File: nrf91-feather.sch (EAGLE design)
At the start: 59 parts, among them J1 CON-USB-1050170001, J2 CON-HEADER-1X12-MALE-PIN, J3 CON-HEADER-1X16-MALE-PIN, J4 1909763-1, J5 104224-0820, J6 CON-S2B-PH-SM4-TB(LF)(SN), J9 CON-0002, Q1 MOSFET-P-SC89, Q2 MOSFET-DUAL-COMP-VMT6, Q3 MOSFET-P-30V-4.3A-SOT23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

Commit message: Adding parallel LDO for low power op. (without need to shut everything off)
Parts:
- removed R4: 100k, wolff-den:RES-100K-1%-0402
- removed R5, R6: 20k, wolff-den:RES-20K-1%-0402
- removed U5: IC-BAV70S, wolff-den:IC-BAV70S
- removed Y1: XTAL-ABS07AIG-32.768KHZ-7-T, wolff-den:XTAL-ABS07AIG-32.768KHZ-7-T
- added C12: 1u, wolff-den:CAP-1U-25V-0402
- C2: value 0.1u -> 1u; device wolff-den:CAP-0.1U-50V-0402 -> wolff-den:CAP-1U-25V-0402
- Q1: value MOSFET-P-SC89 -> MOSFET-N-SC89; device wolff-den:MOSFET-P-SC89 -> wolff-den:MOSFET-N-SC89
- R1: value 100k -> 1M; device wolff-den:RES-100K-1%-0402 -> wolff-den:RES-1M-5%-0402
- U2: value IC-PCF85063ATL/1 -> IC-CP2102N-A02-GQFN20R; device wolff-den:IC-PCF85063ATL/1 -> wolff-den:IC-CP2102N-A02-GQFN20R
- U4: value IC-BAV70S -> (none); device wolff-den:IC-BAV70S -> wolff-den:POWER-VREG-EN-DFN4-1X1
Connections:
- removed net 3V3_EN: R2.2, U3.EN, U4G$1.C, U4G$2.C, U5G$1.C
- removed net N$10: U2.OSCI, Y1.2
- removed net N$18: U2.OSCO, Y1.1
- removed net P0.05/RTC_SCL: R6.1, U1.P0.05, U2.SCL
- removed net P0.06/RTC_SDA: R5.1, U1.P0.06, U2.SDA
- removed net RTC_INT: Q1.G, R4.1, U2.!INT
- removed net RTC_PS_EN: Q1.D, U4G$1.A1
- new net D+: J1.D+, U2.D+
- new net D-: J1.D-, U2.D-
- new net P0.05/USB_UART_RX: U1.P0.05, U2.TXD
- new net P0.06/USB_UART_TX: U1.P0.06, U2.RXD
- net +3V3: now also C2.1, U2.VDD, U4.VOUT; no longer R5.2, R6.2
- net EN: now also R1.1, U4.EN; no longer U5G$1.A2
- net GND: now also C12.2, U2.GND, U4.GND; no longer R1.1, U2.VSS
- net MODE: no longer U5G$1.A1
- net N$9: now also Q1.S, R12.2; no longer R1.2, U2.CLKOE
- net P0.31/NRF_PS_EN: now also R2.2, U3.EN; no longer U4G$1.A2
- net PROG: now also Q1.D; no longer R12.2
- net VBUS: now also Q1.G, U2.VBUS; no longer U4G$2.A2
- net VSYS: now also C12.1, R1.2, U4.VIN; no longer C2.1, Q1.S, R4.2, U2.VDD
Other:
- note added: "LDO for low power op."
- note added: "TODO: en goes low, so does this."
- note added: "TODO: float PROG when USB is not attached."
- note added: "TODO: sleep mode, this if off soemhow"
- note added: "USB to UART"
- note removed: "0.9-5.5V"
- note removed: "Real Time Clock"
- moved on the sheet: C2, C4, C5, C6, C7, L2, R1, R12, R2, U3

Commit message: Current tweaks
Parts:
- added C13, C15: 4.7u, wolff-den:CAP-4.7U-10V-0603
- added C14, C16: 0.1u, wolff-den:CAP-0.1U-50V-0402
- added D5: DIO-TVS-DUAL-CA-1, wolff-den:DIO-TVS-DUAL-CA-1
- added Q5, Q6: MOSFET-N-SC89, wolff-den:MOSFET-N-SC89
- added R15, R16, R5, R6: 100k, wolff-den:RES-100K-1%-0402
- added R4: 1k, wolff-den:RES-1K-1%-0402
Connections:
- removed net D+: J1.D+, U2.D+
- removed net D-: J1.D-, U2.D-
- removed net EN: J2.2, R1.1, U4.EN
- new net !EN: J2.2, Q5.G, Q6.G, R6.1
- new net CP2102N-!RST: R4.1, U2.!RST
- new net CP2102N-VDD: C15.1, C16.1, U2.VDD
- new net CRUMPIT_EN: Q6.D, R1.1, U4.EN
- new net DIFF_N: D5.C2, J1.D-, U2.D-
- new net DIFF_P: D5.C1, J1.D+, U2.D+
- new net N$10: Q5.D, R5.1, U3.EN
- new net N$11: R15.1, R16.2, U2.VBUS
- net +3V3: no longer U2.VDD
- net GND: now also C13.2, C14.2, C15.2, C16.2, D5.A, Q5.S, Q6.S, R16.1, R6.2
- net P0.31/NRF_PS_EN: now also R5.2; no longer U3.EN
- net VBUS: now also C13.1, C14.1, R15.2, R4.2, U2.VREGIN; no longer U2.VBUS
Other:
- note added: "Add divider 22.1k/47.5k"
- note added: "GPS ant"
- note added: "TODO: ESD diodes"
- note added: "TODO: floating this pin necessary?"
- note added: "TODO: how is this handled when VBAT <= 3.0V"
- note added: "TODO: jumper (defualt soldered) to VBAT"
- note removed: "TODO: en goes low, so does this."
- note removed: "TODO: sleep mode, this if off soemhow"
- moved on the sheet: R2

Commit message: Removing LDO. Cleaning up traces. Fixing slot issue! Adding timer back.
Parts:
- removed D5: DIO-TVS-DUAL-CA-1, wolff-den:DIO-TVS-DUAL-CA-1
- removed Q6: MOSFET-N-SC89, wolff-den:MOSFET-N-SC89
- removed R1: 1M, wolff-den:RES-1M-5%-0402
- added C17: 0.1u, wolff-den:CAP-0.1U-50V-0402
- added J7: 1909763-1, wolff-den:1909763-1
- added L3, L4: 3.9n, wolff-den:IND-3.9NH-170MA-0402
- added R17, R18: 20k, wolff-den:RES-20K-1%-0402
- added U5: IC-TPD4S012DRYR, wolff-den:IC-TPD4S012DRYR
- added U8: IC-PCF85063ATL/1, wolff-den:IC-PCF85063ATL/1
- added U9: IC-BAV70S, wolff-den:IC-BAV70S
- added Y1: XTAL-ABS07AIG-32.768KHZ-7-T, wolff-den:XTAL-ABS07AIG-32.768KHZ-7-T
- C12: value 1u -> 100p; device wolff-den:CAP-1U-25V-0402 -> wolff-den:CAP-100P-50V-0402
- C2: value 1u -> 0.1u; device wolff-den:CAP-1U-25V-0402 -> wolff-den:CAP-0.1U-50V-0402
- Q1: value MOSFET-N-SC89 -> MOSFET-P-SC89; device wolff-den:MOSFET-N-SC89 -> wolff-den:MOSFET-P-SC89
- U4: value (none) -> BGU6005,115; device wolff-den:POWER-VREG-EN-DFN4-1X1 -> wolff-den:BGU6005,115
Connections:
- net N$10 renamed PS_EN
- net N$3 renamed ANT
- removed net CRUMPIT_EN: Q6.D, R1.1, U4.EN
- removed net N$9: Q1.S, R12.2
- new net GPS: U1.GPS, U4.RF_OUT
- new net GPS_AMP: L3.2, U4.RF_IN
- new net GPS_CON: J7.SIG, L3.1
- new net LNA_EN: U1.COEX0, U4.ENABLE
- new net N$10: U8.OSCI, Y1.2
- new net N$18: U8.OSCO, Y1.1
- new net PS_EN_CC: R2.2, R5.2, U9G$1.C, U9G$2.C
- new net RTC_INT: Q1.G, R6.1, U8.!INT
- new net RTC_PS_EN: Q1.D, U9G$2.A2
- new net VCC_LNA_FILT: C12.1, C2.1, L4.2, U4.VCC
- net !EN: no longer Q6.G, R6.1
- net +3V3: now also L4.1, R17.2, R18.2; no longer C2.1, U4.VOUT
- net DIFF_N: now also U5.D-; no longer D5.C2
- net DIFF_P: now also U5.D+; no longer D5.C1
- net GND: now also C17.2, J7.GND, U4.GND1, U4.GND2, U5.GND, U8.CLKOE, U8.VSS; no longer D5.A, Q6.S, R6.2, U4.GND
- net MODE: now also U9G$2.A1
- net P0.26/SDA: now also R17.1, U8.SDA
- net P0.27/SCL: now also R18.1, U8.SCL
- net P0.31/NRF_PS_EN: now also U9G$1.A1; no longer R2.2, R5.2
- net PROG: now also R12.2; no longer Q1.D
- net VBUS: now also U5.VBUS, U9G$1.A2; no longer Q1.G
- net VSYS: now also C17.1, Q1.S, R6.2, U8.VDD; no longer C12.1, R1.2, U4.VIN
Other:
- note added: "0.9-5.5V"
- note added: "2.7-3.6V (abs max 4.6)"
- note added: "Change divider values 22.1k/47.5k"
- note added: "Note: LNA is enabled when COEX is turned on"
- note added: "Real Time Clock"
- note added: "TODO: check ref layout"
- note added: "TODO: make inductors both 5.6"
- note removed: "2.7-3.6V"
- note removed: "Add divider 22.1k/47.5k"
- note removed: "LDO for low power op."
- note removed: "TODO: -- * Charger * Blue LED * JST * Programming header * Built in RTC for Wake from Sleep * Flash * USB Connector * Reset Button * Mode Button"
- note removed: "TODO: ESD diodes"
- note removed: "TODO: float PROG when USB is not attached."
- note removed: "TODO: floating this pin necessary?"
- note removed: "TODO: how is this handled when VBAT <= 3.0V"
- note removed: "TODO: jumper (defualt soldered) to VBAT"

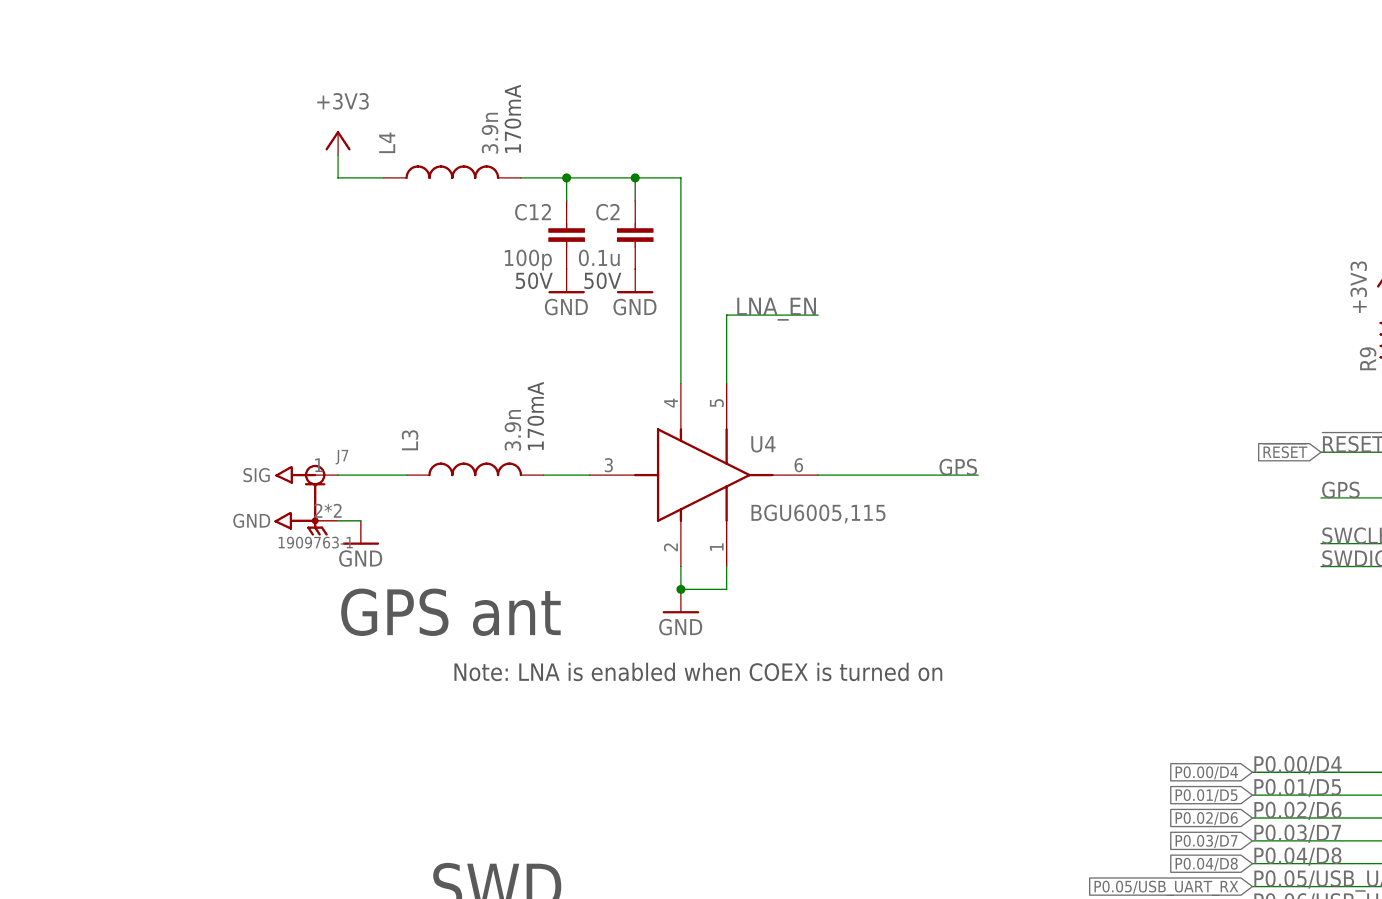
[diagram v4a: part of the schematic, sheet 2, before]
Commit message: 1. Clean  up silk 2. Updated 3D packages 3. Pushed to OSH Park + Fusion 4. Added 1.8V LDO for LNA
Proto2
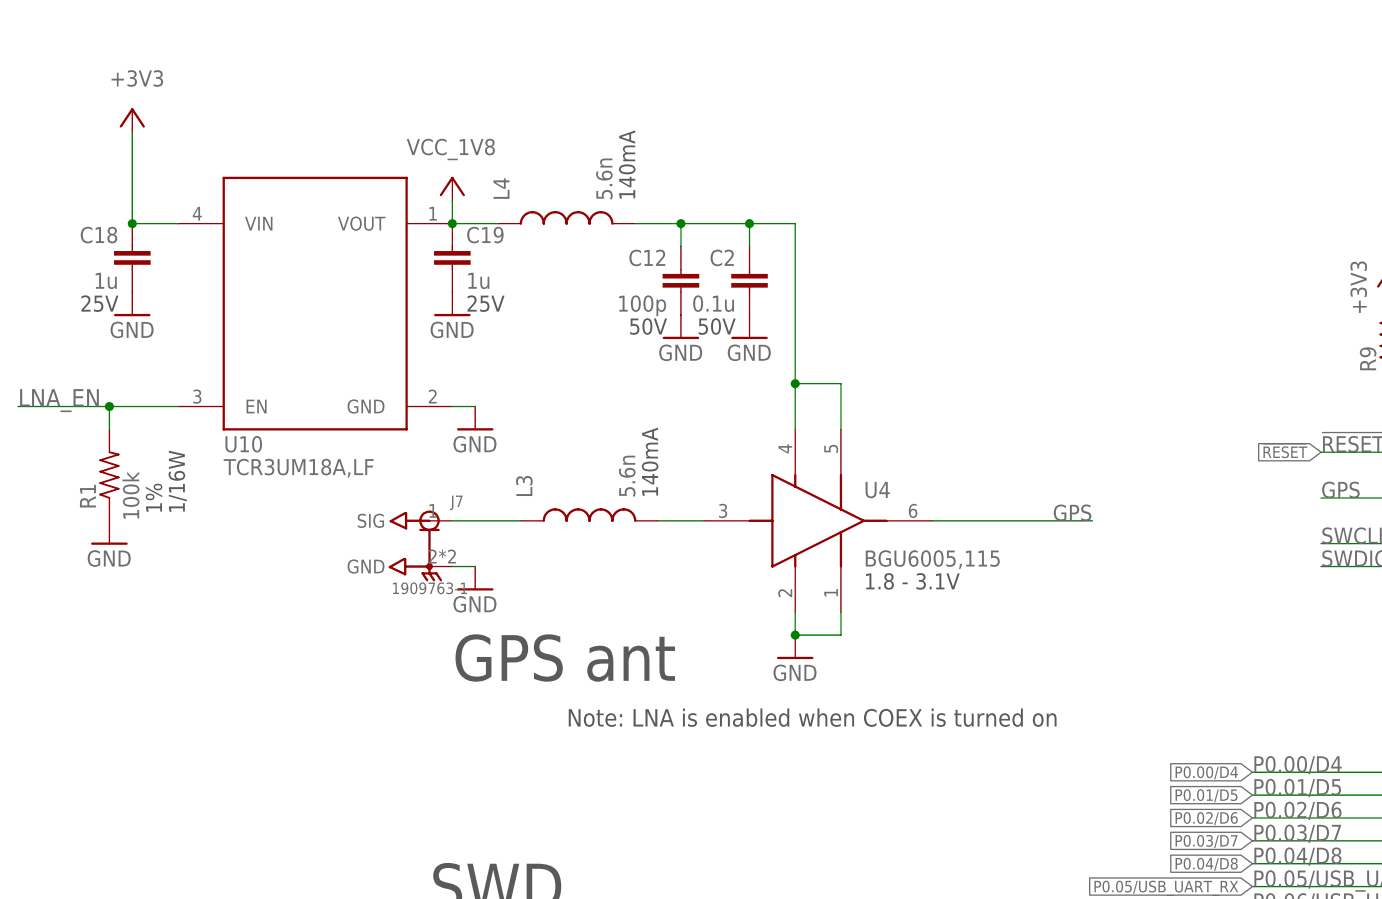
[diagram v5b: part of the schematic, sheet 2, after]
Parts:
- added C18, C19: 1u, wolff-den:CAP-1U-25V-0402
- added R1: 100k, wolff-den:RES-100K-1%-0402
- added U10: (no value), wolff-den:POWER-VREG-EN-1.8V-DFN4-1X1
- L3, L4: value 3.9n -> 5.6n; device wolff-den:IND-3.9NH-170MA-0402 -> wolff-den:IND-5.6NH-140MA-0402
- R15: value 100k -> 22.1k; device wolff-den:RES-100K-1%-0402 -> wolff-den:RES-22.1K-1%-0402
- R16: value 100k -> 47.5k; device wolff-den:RES-100K-1%-0402 -> wolff-den:RES-47.5K-1%-0402
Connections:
- new net VCC_1V8: C19.1, L4.1, U10.VOUT
- net +3V3: now also C18.1, U10.VIN; no longer L4.1
- net GND: now also C18.2, C19.2, R1.1, U10.GND
- net LNA_EN: now also R1.2, U10.EN; no longer U4.ENABLE
- net VCC_LNA_FILT: now also U4.ENABLE
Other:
- note added: "1.8 - 3.1V"
- note removed: "Change divider values 22.1k/47.5k"
- note removed: "TODO: check ref layout"
- note removed: "TODO: make inductors both 5.6"
- moved on the sheet: C12, C2, J7, L3, L4, R15, U4

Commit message: 1. Changing name of design to nRF9160 Feather 2. Fixing holes with BOM export.
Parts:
- added SOLDER1: SOLDER-PASTE-ROOM-TEMP-50G, wolff-den:SOLDER-PASTE-ROOM-TEMP-50G
- C10, C13, C15, C3, C8: device wolff-den:CAP-4.7U-10V-0603 -> wolff-den:CAP-4.7U-6.3V-0603
- PCB1: value PCB-SARA-R410-02B -> PCB-NRF91-FEATHER; device wolff-den:PCB-SARA-R410-02B -> wolff-den:PCB-NRF91-FEATHER
- R4: device wolff-den:RES-1K-1%-0402 -> wolff-den:RES-1K-5%-0402

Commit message: 1. Adding pulldown on EN pin
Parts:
- added R19: 1M, wolff-den:RES-1M-5%-0402
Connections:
- net !EN: now also R19.2
- net GND: now also R19.1
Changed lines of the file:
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@@
 <attribute name="MQTY" value="150"/>
 </part>
+<part name="R19" library="wolff-den" library_urn="urn:adsk.eagle:library:6370453" deviceset="RES" device="-0402" package3d_urn="urn:adsk.eagle:package:19061974/2" technology="-1M-5%" value="1M"/>
+<part name="GND46" library="supply1" library_urn="urn:adsk.eagle:library:371" deviceset="GND" device=""/>
 </parts>
 <sheets>
@@
 <attribute name="NAME" x="10.16" y="17.78" size="1.778" layer="95"/>
 </instance>
+<instance part="R19" gate="G$1" x="86.36" y="177.8" smashed="yes" rot="MR90">
+<attribute name="NAME" x="87.8586" y="173.99" size="1.778" layer="95" rot="MR90"/>
+<attribute name="VALUE" x="83.058" y="172.72" size="1.778" layer="96" rot="MR90"/>
+<attribute name="TOLERANCE" x="80.518" y="173.482" size="1.778" layer="97" rot="MR90"/>
+<attribute name="POWER" x="77.978" y="173.482" size="1.778" layer="97" rot="MR90"/>
+</instance>
+<instance part="GND46" gate="1" x="86.36" y="170.18" smashed="yes">
+<attribute name="VALUE" x="83.82" y="167.64" size="1.778" layer="96"/>
+</instance>
 </instances>
 <busses>
@@
 <pinref part="U5" gate="G$1" pin="GND"/>
 <wire x1="111.76" y1="101.6" x2="114.3" y2="101.6" width="0.1524" layer="91"/>
+</segment>
+<segment>
+<pinref part="R19" gate="G$1" pin="1"/>
+<pinref part="GND46" gate="1" pin="GND"/>
 </segment>
 </net>
@@
 </segment>
 <segment>
-<wire x1="91.44" y1="182.88" x2="73.66" y2="182.88" width="0.1524" layer="91"/>
+<wire x1="91.44" y1="182.88" x2="86.36" y2="182.88" width="0.1524" layer="91"/>
 <label x="73.66" y="182.88" size="1.9304" layer="95"/>
 <pinref part="Q5" gate="A" pin="G"/>
-</segment>
-</net>
+<pinref part="R19" gate="G$1" pin="2"/>
+<wire x1="86.36" y1="182.88" x2="73.66" y2="182.88" width="0.1524" layer="91"/>
+<junction x="86.36" y="182.88"/>
+</segment>
+</net>

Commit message: Using internal switch to route GPS signal.
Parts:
- removed C19: 1u, wolff-den:CAP-1U-25V-0402
- removed J7: 1909763-1, wolff-den:1909763-1
- removed L3, L4: 5.6n, wolff-den:IND-5.6NH-140MA-0402
- removed U10: (no value), wolff-den:POWER-VREG-EN-1.8V-DFN4-1X1
- added ASSEMBLY1: ASSY-COST-NRF91-FEATHER, wolff-den:ASSY-COST-NRF91-FEATHER
- added C20, C21, C22: 15p, wolff-den:CAP-15P-50V-0402
- added L5: 39n, wolff-den:IND-39NH-250MA-0402
- added LOGO1: LOGO-MROHM, wolff-den:LOGO-MROHM
- C11: device wolff-den:CAP-1U-25V-0402 -> wolff-den:CAP-1U-10V-0402
- C18: value 1u -> 0.1u; device wolff-den:CAP-1U-25V-0402 -> wolff-den:CAP-0.1U-50V-0402
- J4: value 1909763-1 -> CON-1909763-1; device wolff-den:1909763-1 -> wolff-den:CON-1909763-1
- J5: value 104224-0820 -> CON-SIM-104224-0820; device wolff-den:104224-0820 -> wolff-den:CON-SIM-104224-0820
- J9: value CON-0002 -> CON-TC2030-MCP-NL; device wolff-den:CON-0002 -> wolff-den:CON-TC2030-MCP-NL
- Q3: value MOSFET-P-30V-4.3A-SOT23 -> MOSFET-P-20V-4.7A-SOT23; device wolff-den:MOSFET-P-30V-4.3A-SOT23 -> wolff-den:MOSFET-P-20V-4.7A-SOT23
- R1: value 100k -> 1M; device wolff-den:RES-100K-1%-0402 -> wolff-den:RES-1M-5%-0402
- SW1, SW2: value SW-EVP-AA402W -> SW-SPST-NO-KMR6; device wolff-den:SW-EVP-AA402W -> wolff-den:SW-SPST-NO-KMR6
- U4: value BGU6005,115 -> IC-LNA-BGA725L6-TSLP6-2; device wolff-den:BGU6005,115 -> wolff-den:IC-LNA-BGA725L6-TSLP6-2
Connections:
- net FLASH_CS renamed P0.07/FLASH_CS
- net FLASH_HOLD renamed P0.10/FLASH_HOLD
- net FLASH_SCK renamed P0.11/FLASH_SCK
- net FLASH_SI renamed P0.09/FLASH_SI
- net FLASH_SO renamed P0.28/FLASH_SO
- net FLASH_WP renamed P0.08/FLASH_WP
- removed net GPS_AMP: L3.2, U4.RF_IN
- removed net GPS_CON: J7.SIG, L3.1
- removed net VCC_1V8: C19.1, L4.1, U10.VOUT
- removed net VCC_LNA_FILT: C12.1, C2.1, L4.2, U4.ENABLE, U4.VCC
- new net AUX: C21.1, L5.2, U1.AUX
- new net AUX_FILT: C21.2, C22.1, U4.RF_IN
- net +3V3: now also C12.1, C2.1, U4.VCC; no longer C18.1, U10.VIN
- net ANT: now also C20.1
- net GND: now also C20.2, C22.2, L5.1; no longer C19.2, J7.GND, U10.GND
- net LNA_EN: now also C18.1, U4.ENABLE; no longer U10.EN
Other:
- moved on the sheet: C1, C12, C18, C2, L1, R1, U4
